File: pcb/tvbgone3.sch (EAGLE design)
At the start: 32 parts, among them Q1 MMBT5088, Q2 MMBT5088, Q3 MMBT5088, Q4 MMBT5088, Q5 MMBT4403, Q6 MOSFET-NCHANNELBSS123LT1G, Q7 MOSFET-NCHANNELBSS123LT1G, U1 ATTINY85V-10SU, U3 MCP73831

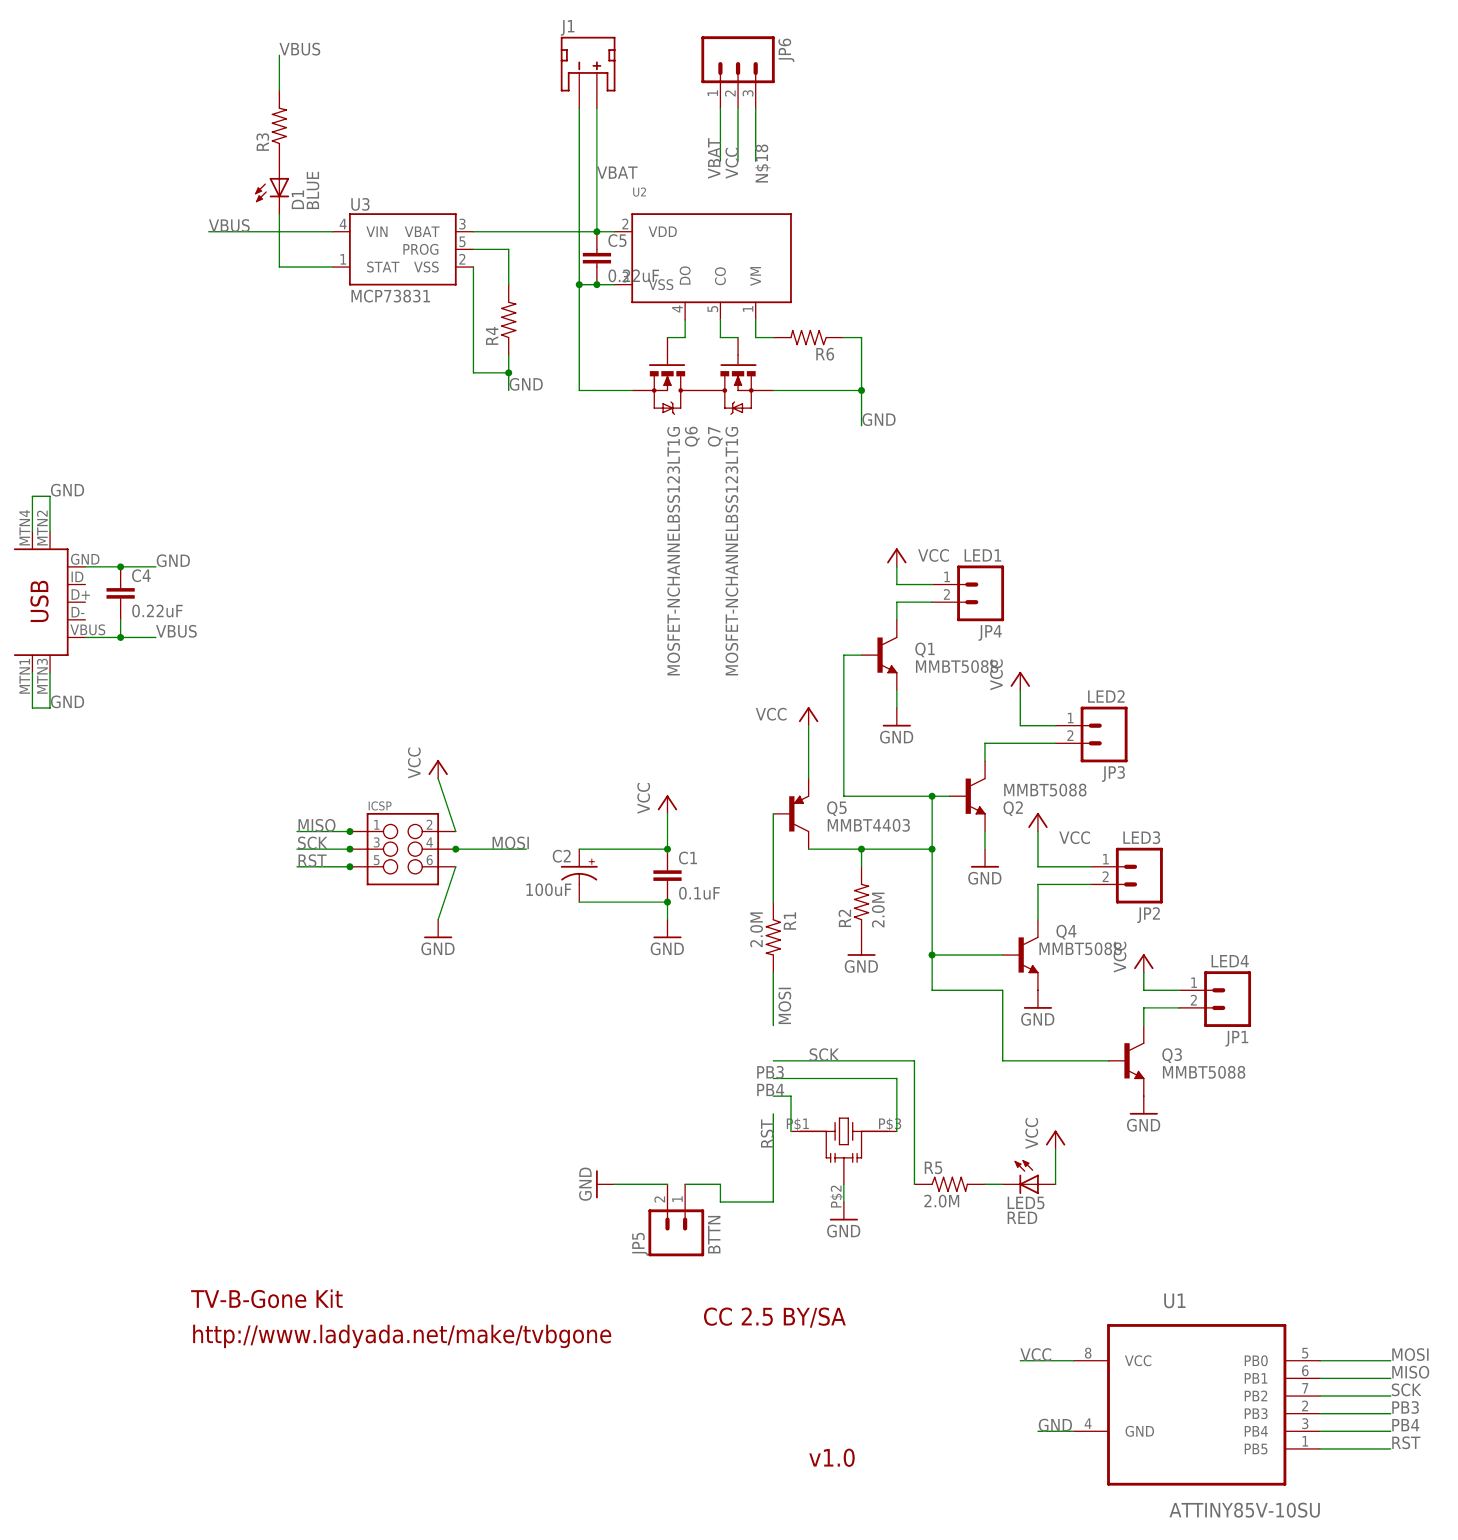
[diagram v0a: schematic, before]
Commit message: finalized version 1 of smd board and documented the fuses. Tested. It Works\!
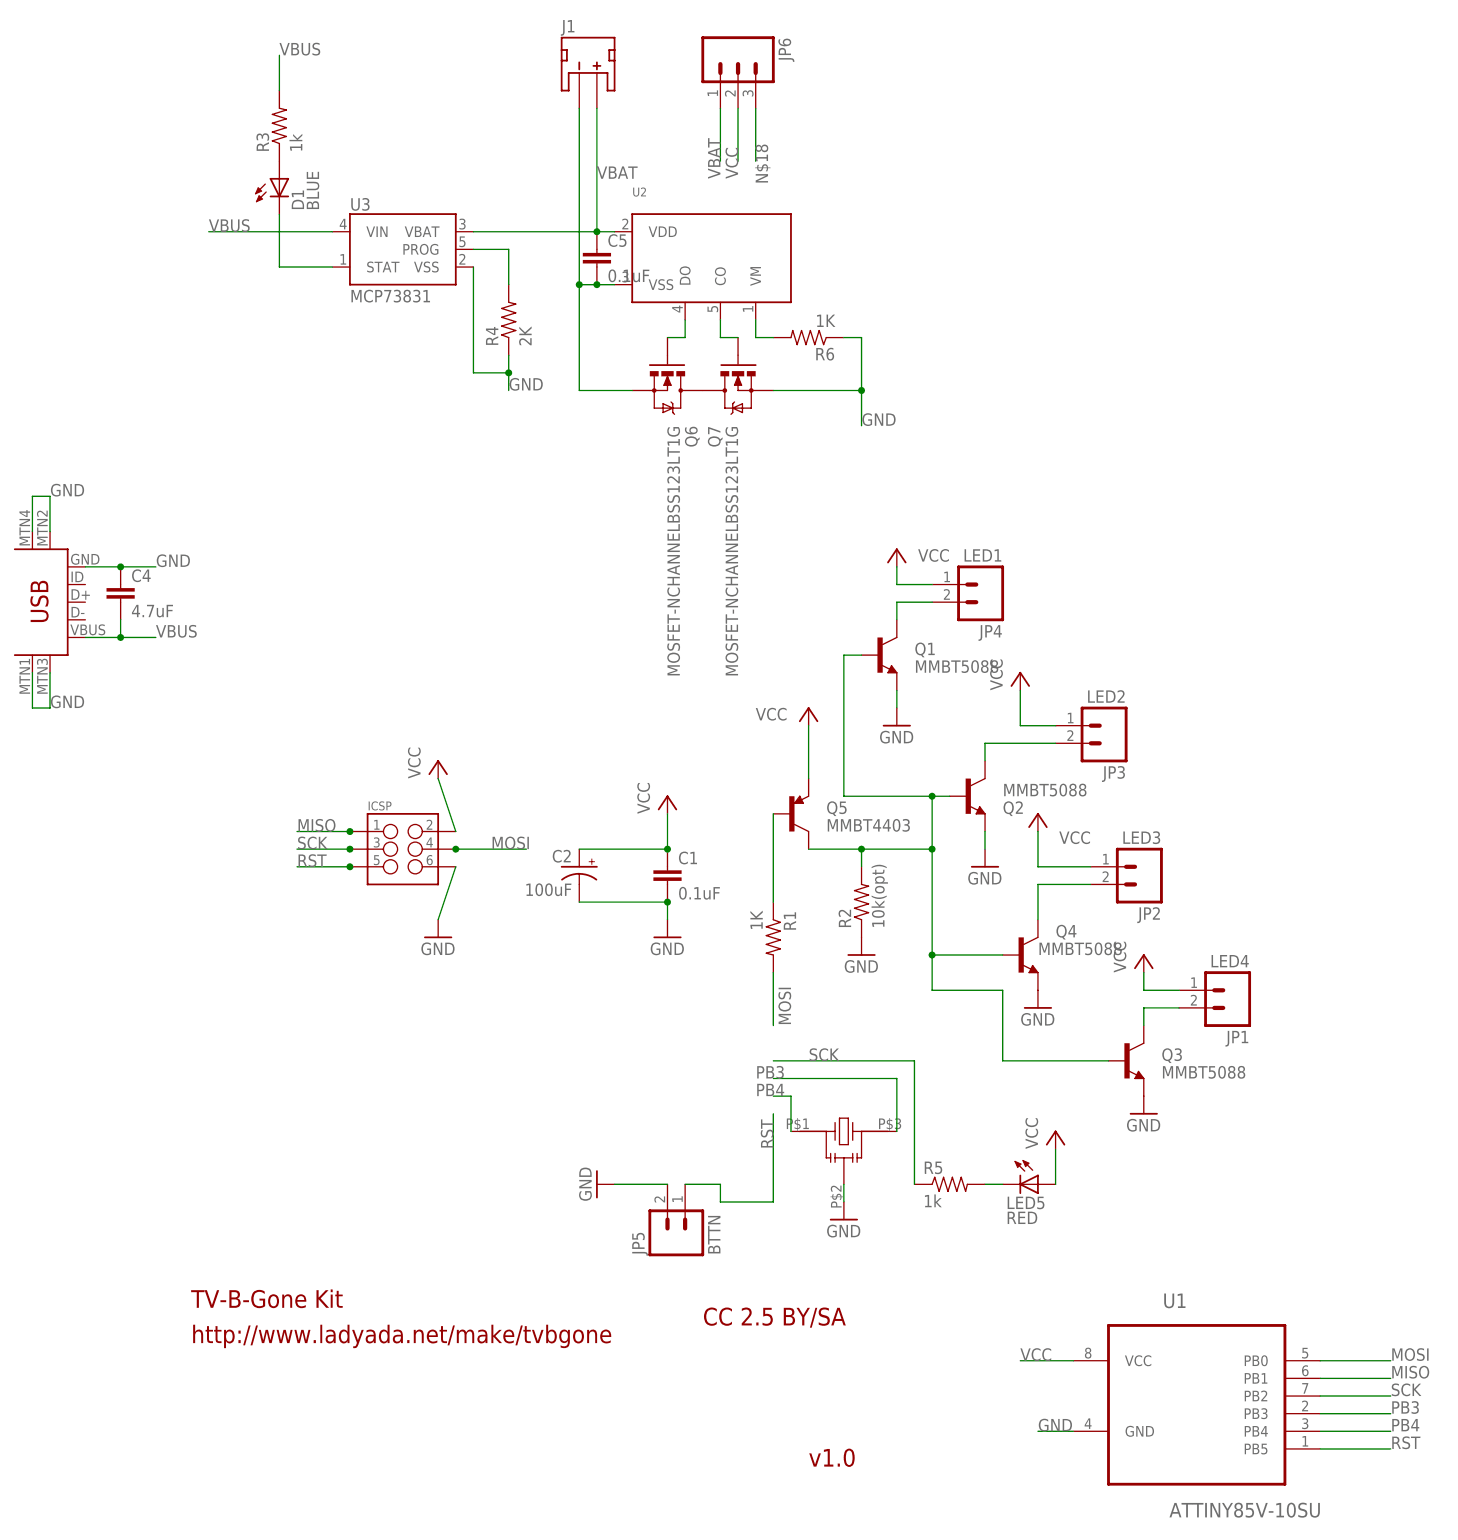
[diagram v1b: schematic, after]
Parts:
- C4: value 0.22uF -> 4.7uF
- C5: value 0.22uF -> 0.1uF
- R1: value 2.0M -> 1K
- R2: value 2.0M -> 10k(opt)
- R3: value (none) -> 1k
- R4: value (none) -> 2K
- R5: value 2.0M -> 1k
- R6: value (none) -> 1K
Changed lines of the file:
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@@
 <part name="LED5" library="SparkFun-LED" deviceset="LED" device="0603" value="RED"/>
 <part name="P+6" library="supply1" deviceset="VCC" device=""/>
-<part name="R5" library="SparkFun-Resistors" deviceset="2MOHMS-1/10W-1%(0603)" device="" value="2.0M"/>
+<part name="R5" library="SparkFun-Resistors" deviceset="2MOHMS-1/10W-1%(0603)" device="" value="1k"/>
 <part name="GND8" library="supply1" deviceset="GND" device=""/>
 <part name="P+7" library="supply1" deviceset="VCC" device=""/>
@@
 <part name="P+9" library="supply1" deviceset="VCC" device=""/>
 <part name="GND10" library="supply1" deviceset="GND" device=""/>
-<part name="R2" library="SparkFun-Resistors" deviceset="2MOHMS-1/10W-1%(0603)" device="" value="2.0M"/>
-<part name="R1" library="SparkFun-Resistors" deviceset="2MOHMS-1/10W-1%(0603)" device="" value="2.0M"/>
+<part name="R2" library="SparkFun-Resistors" deviceset="2MOHMS-1/10W-1%(0603)" device="" value="10k(opt)"/>
+<part name="R1" library="SparkFun-Resistors" deviceset="2MOHMS-1/10W-1%(0603)" device="" value="1K"/>
 <part name="P+10" library="supply1" deviceset="VCC" device=""/>
 <part name="Q5" library="SparkFun-DiscreteSemi" deviceset="TRANSISTOR_PNP" device="MMBT4403" value="MMBT4403"/>
@@
 <part name="U3" library="electric_imp" deviceset="MCP73831" device=""/>
 <part name="U$2" library="SparkFun-Connectors" deviceset="USB-MINIB" device="-5PIN"/>
-<part name="R3" library="SparkFun-Resistors" deviceset="3.3MOHM-1/10W-1%(0603)" device=""/>
+<part name="R3" library="SparkFun-Resistors" deviceset="3.3MOHM-1/10W-1%(0603)" device="" value="1k"/>
 <part name="D1" library="SparkFun-LED" deviceset="LED-BLUE" device="0603" value="BLUE"/>
 <part name="Q6" library="electric_imp" deviceset="MOSFET-NCHANNEL" device="BSS123LT1G"/>
-<part name="C4" library="SparkFun-Capacitors" deviceset="0.22UF50V-20%,+80%(0603)" device="" value="0.22uF"/>
-<part name="R4" library="SparkFun-Resistors" deviceset="3.3MOHM-1/10W-1%(0603)" device=""/>
-<part name="C5" library="SparkFun-Capacitors" deviceset="0.22UF50V-20%,+80%(0603)" device="" value="0.22uF"/>
+<part name="C4" library="SparkFun-Capacitors" deviceset="0.22UF50V-20%,+80%(0603)" device="" value="4.7uF"/>
+<part name="R4" library="SparkFun-Resistors" deviceset="3.3MOHM-1/10W-1%(0603)" device="" value="2K"/>
+<part name="C5" library="SparkFun-Capacitors" deviceset="0.22UF50V-20%,+80%(0603)" device="" value="0.1uF"/>
 <part name="Q7" library="electric_imp" deviceset="MOSFET-NCHANNEL" device="BSS123LT1G"/>
-<part name="R6" library="SparkFun-Resistors" deviceset="3.3MOHM-1/10W-1%(0603)" device=""/>
+<part name="R6" library="SparkFun-Resistors" deviceset="3.3MOHM-1/10W-1%(0603)" device="" value="1K"/>
 <part name="JP6" library="SparkFun-Connectors" deviceset="M03" device="SMD_RA_MALE"/>
 </parts>
